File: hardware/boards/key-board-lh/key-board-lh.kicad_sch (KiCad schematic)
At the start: 24 parts

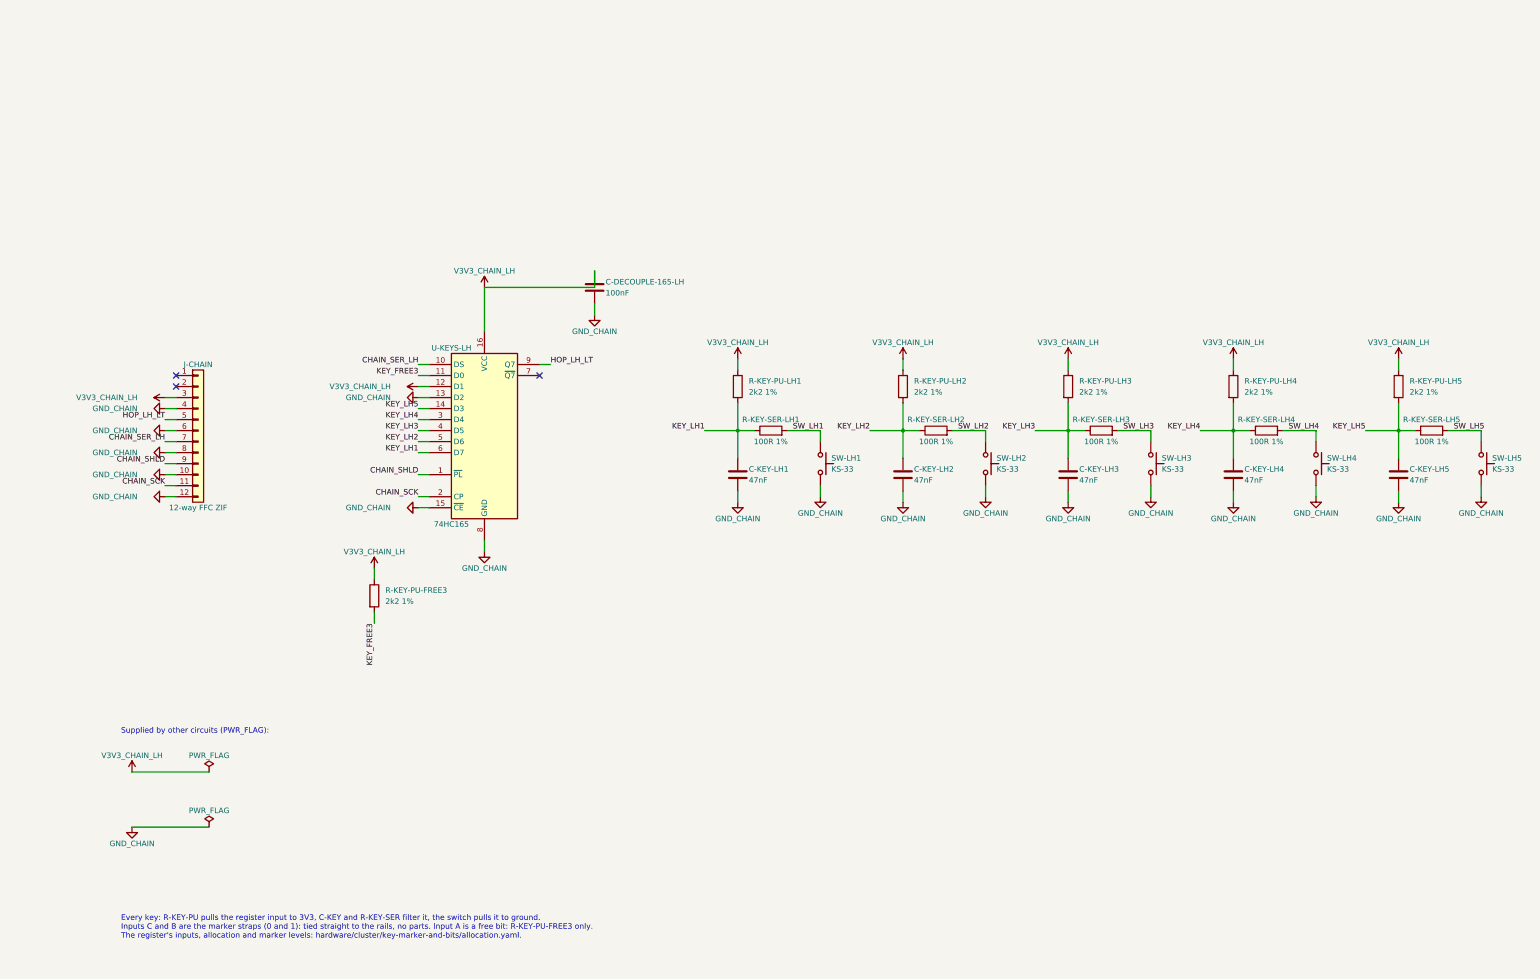
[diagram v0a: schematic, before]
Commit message: KiCad sheets are the source of truth (ADR 0019): key-board circuits and boards migrated
- The circuit sheets key-register, key-switch-network and
  key-marker-and-bits own their connections and part facts (fields Row,
  Pins, Pins_source, Note; ports as hierarchical labels). Their
  netlist.yaml is now EXPORTED by tools/kicad.py.
- key-board-rh and key-board-lh are KiCad projects placing those sheets
  once per instance (register, one per key, one per free bit); their
  board-netlist.yaml is exported, with KiCad's ERC over the hierarchy.
- Proved: every exported circuit netlist equals the hand-written one it
  replaces, part by part and net by net; both KiCad boards equal the
  boards the retired tools/board.py assembled. ERC clean.
- key-marker-and-bits is now one free-bit pull-up, replicated 3; marker
  straps are board wiring. nets.yaml gains FREE_BIT.
- tools/kicad.py check: stale exports, stale or edited renders
  (hardware/SHEETS.csv), board ERC, and board wiring vs allocation.yaml vs
  the page table vs key-layout.yaml. Tested: an unexported edit and a
  swapped key both fail.
- CLAUDE.md, hardware/README.md, repo-maintenance.md and tooling.md say
  what is source and what is exported. tools/board.py retired.

Co-Authored-By: Claude Opus 5.5 <noreply@anthropic.com>
Claude-Session: https://claude.ai/code/session_01LmB4muFXnoLprWX4JzuJ5A
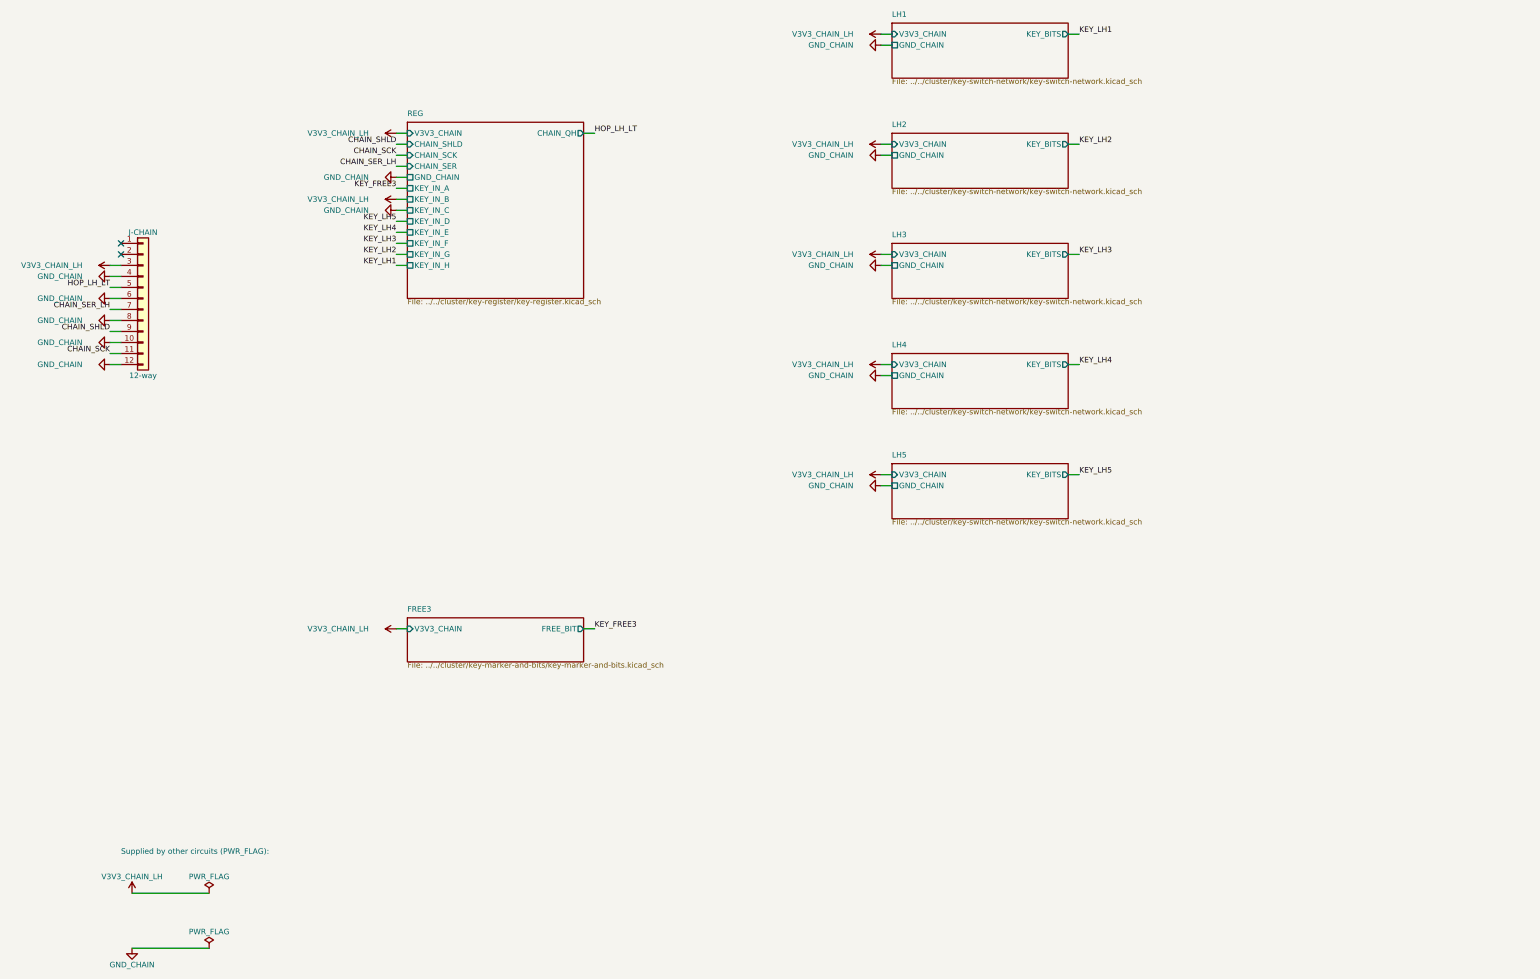
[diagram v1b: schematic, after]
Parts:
- removed C-DECOUPLE-165-LH: 100nF, symbol Device:C
- removed C-KEY-LH1, C-KEY-LH2, C-KEY-LH3, C-KEY-LH4, C-KEY-LH5: 47nF, symbol Device:C
- removed R-KEY-PU-FREE3, R-KEY-PU-LH1, R-KEY-PU-LH2, R-KEY-PU-LH3, R-KEY-PU-LH4, R-KEY-PU-LH5: 2k2 1%, symbol Device:R
- removed R-KEY-SER-LH1, R-KEY-SER-LH2, R-KEY-SER-LH3, R-KEY-SER-LH4, R-KEY-SER-LH5: 100R 1%, symbol Device:R
- removed SW-LH1, SW-LH2, SW-LH3, SW-LH4, SW-LH5: KS-33, symbol Switch:SW_Push
- removed U-KEYS-LH: 74HC165, symbol 74xx:74HC165
- J-CHAIN: value 12-way FFC ZIF -> 12-way; Note (none) -> left_hand key board. REVERSED, like the right_hand one; Pins (none) -> 1=1 2=2 3=3 4=4 5=5 6=6 7=7 8=8 9=9 10=10 11=11 12=12; Row (none) -> J-CHAIN
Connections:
- no-connect marks 3 -> 2
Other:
- added sheet FREE3 (../../cluster/key-marker-and-bits/key-marker-and-bits.kicad_sch)
- added sheet LH1 (../../cluster/key-switch-network/key-switch-network.kicad_sch)
- added sheet LH2 (../../cluster/key-switch-network/key-switch-network.kicad_sch)
- added sheet LH3 (../../cluster/key-switch-network/key-switch-network.kicad_sch)
- added sheet LH4 (../../cluster/key-switch-network/key-switch-network.kicad_sch)
- added sheet LH5 (../../cluster/key-switch-network/key-switch-network.kicad_sch)
- added sheet REG (../../cluster/key-register/key-register.kicad_sch)
- note removed: "Every key: R-KEY-PU pulls the register input to 3V3, C-KEY and R-KEY-SER filter it, the switch pulls it to ground. Inputs C and B are the marker straps (0 and 1): tied straight to the rails, no parts. Input A is a free bit: R-KEY-PU-FREE3 only. The register's inputs, allocation and marker levels: hardware/cluster/key-marker-and-bits/allocation.yaml."
- title: Left-hand key board (PCB-CLUSTER, left_hand) -> Left-hand key board (left_hand cluster, PCB-CLUSTER)
- moved on the sheet: J-CHAIN

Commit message: First PCB: the left-hand key board, placed from the body CAD and routed
- tools/pcb.py: a board's first layout from its KiCad sheets (netlist,
  footprints) and the body CAD's new exports (key-board outline DXF,
  switch and ribbon-connector positions); then the .kicad_pcb is source.
  check = KiCad DRC with schematic parity + switches where the CAD puts
  them; render = 3D both sides, 2D copper, and fab/ (Gerbers, drill,
  placement), ledgered in hardware/SHEETS.csv. tools/kicad.py check runs it.
- tools/pcb_route.py: a small two-layer grid router for simple boards;
  ground routed as a net plus pours and stitching vias.
- key-board-lh: 24 parts, all nets routed; KiCad DRC 0 errors, schematic
  parity clean (one stock-footprint silkscreen warning). Tested: a switch
  moved 1 mm fails the check.
- Footprints on the sheets; hardware/lib/woody.pretty holds the KS-33
  footprint (marbastlib, banked) with Gateron's STEP lifted by
  switch.pcb_below_seat. J-CHAIN's stand-in is Molex 200528-0120.
- Findings, recorded in tooling.md §4 and DESIGN.md: the ribbon connector
  needs 6.7 mm, the CAD envelope is 5.5; KS-33 pins show only ~0.1 mm
  below a 1.6 mm board (1.2 mm would leave ~0.5).
- setup-env.sh installs footprints, rsvg, shapely and repairs an empty
  global fp-lib-table.

Co-Authored-By: Claude Opus 5.5 <noreply@anthropic.com>
Claude-Session: https://claude.ai/code/session_01LmB4muFXnoLprWX4JzuJ5A
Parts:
- J-CHAIN: footprint (none) -> Connector_FFC-FPC:Molex_200528-0120_1x12-1MP_P1.00mm_Horizontal
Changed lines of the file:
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@@
     (property "Reference" "J-CHAIN" (at 45.72 86.36 0) (effects (font (size 1.27 1.27))))
     (property "Value" "12-way" (at 45.72 119.38 0) (effects (font (size 1.27 1.27))))
-    (property "Footprint" "" (at 45.72 101.6 0) (effects (font (size 1.27 1.27)) hide))
+    (property "Footprint" "Connector_FFC-FPC:Molex_200528-0120_1x12-1MP_P1.00mm_Horizontal" (at 45.72 101.6 0) (effects (font (size 1.27 1.27)) hide))
     (property "Datasheet" "" (at 45.72 101.6 0) (effects (font (size 1.27 1.27)) hide))
     (property "Row" "J-CHAIN" (at 45.72 101.6 0) (effects (font (size 1.27 1.27)) hide))

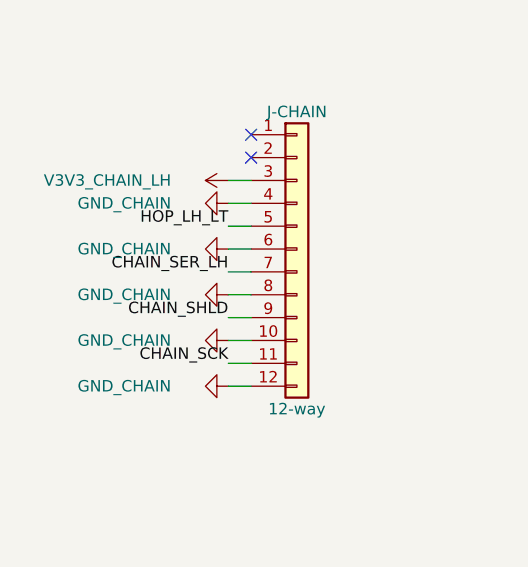
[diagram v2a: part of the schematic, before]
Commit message: Key chain on through-hole 1.27 mm IDC: model, key boards, router fix
The owner's choice (option 2): a right-angle 2x6 1.27 mm shrouded IDC header
on each board (Samtec SHF-106-01-L-D-RA stand-in), the key board's hanging
over the main board's, and a flat IDC ribbon long enough to plug in with the
lid laid beside the body - closed, a flat hairpin along the body, clear of
the LED strip.

- CAD: chain headers, plugs and the hairpin ribbon replace the ZIF/FFC C;
  positions found clear of every switch's pole and pins and the regulator
  block; ribbon length derived from the service position (drc.echo); a plate
  window over the key header's pin tails. body.yaml boards.chain_* and
  routing.chain_* replace ffc_*. 0 DRC FAILs, 0 clashes over 134 solids.
- Key boards: J-CHAIN footprint woody:IDC-Header_2x06_P1.27mm_Samtec_SHF_
  Horizontal (new); pinout moved one pin for the upside-down header (main
  pin n -> key pin 12-n odd / 14-n even); ERC clean. The interface netlist
  follows and agrees pin for pin.
- pcb.py places J-CHAIN from the CAD's "chain" line and checks it; the
  router no longer walls a plated pad off from its own track (1.27 mm pads).
  LH board: DRC 0 errors, parity clean; renders and fab/ regenerated.

The BOM rows, the key-chain page and the ADR 0017 amendment follow in the
next commit.

Co-Authored-By: Claude Opus 5.5 <noreply@anthropic.com>
Claude-Session: https://claude.ai/code/session_01LmB4muFXnoLprWX4JzuJ5A
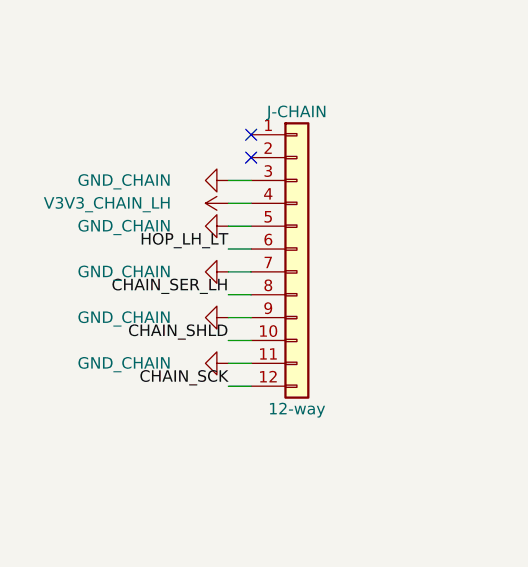
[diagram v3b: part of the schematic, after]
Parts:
- J-CHAIN: footprint Connector_FFC-FPC:Molex_200528-0120_1x12-1MP_P1.00mm_Horizontal -> woody:IDC-Header_2x06_P1.27mm_Samtec_SHF_Horizontal; Note left_hand key board. REVERSED, like the right_hand one -> key-board end of the chain ribbon: 1.27 mm IDC, right-angle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
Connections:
- net CHAIN_SCK: now also J-CHAIN.12 (Pin_12); no longer J-CHAIN.11 (Pin_11)
- net CHAIN_SER_LH: now also J-CHAIN.8 (Pin_8); no longer J-CHAIN.7 (Pin_7)
- net CHAIN_SHLD: now also J-CHAIN.10 (Pin_10); no longer J-CHAIN.9 (Pin_9)
- net GND_CHAIN: now also J-CHAIN.11 (Pin_11), J-CHAIN.3 (Pin_3), J-CHAIN.5 (Pin_5), J-CHAIN.7 (Pin_7), J-CHAIN.9 (Pin_9); no longer J-CHAIN.10 (Pin_10), J-CHAIN.12 (Pin_12), J-CHAIN.4 (Pin_4), J-CHAIN.6 (Pin_6), J-CHAIN.8 (Pin_8)
- net HOP_LH_LT: now also J-CHAIN.6 (Pin_6); no longer J-CHAIN.5 (Pin_5)
- net V3V3_CHAIN_LH: now also J-CHAIN.4 (Pin_4); no longer J-CHAIN.3 (Pin_3)

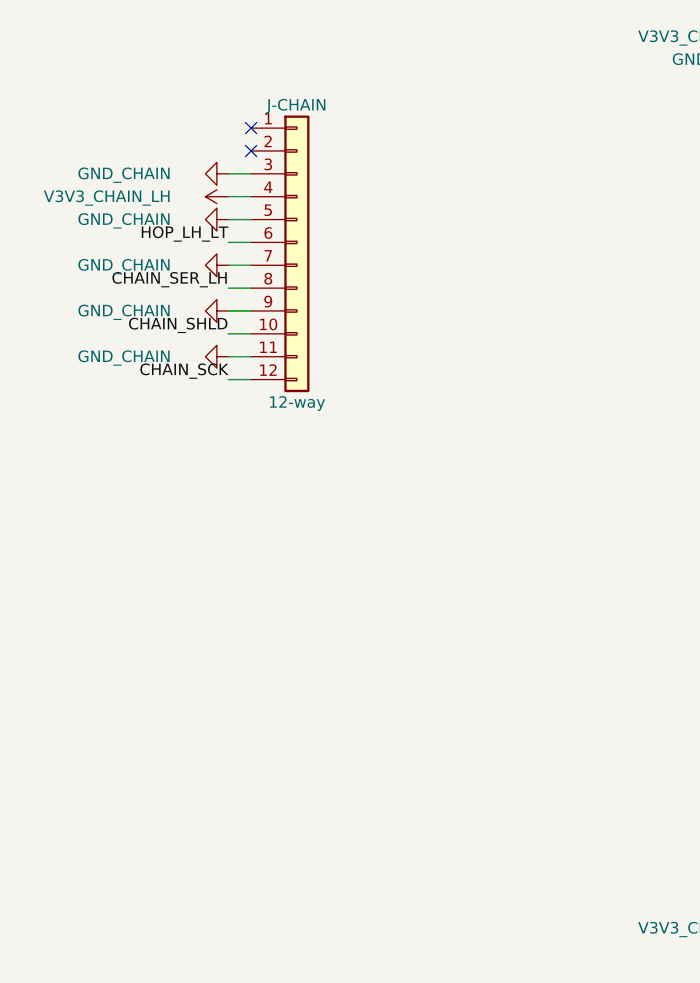
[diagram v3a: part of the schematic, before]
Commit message: LH key board as the worked example: orderable, labelled, testable
- Samtec full prints banked (SHF header, FFSD cable); the header's true
  dimensions replace the catalogue estimates (body.yaml boards.chain_*), and
  the cable is ordered -RN2 (notch reversed on the key-board end): both
  sockets' cables leave downward, the ribbon runs flat, and key-board pin =
  13 - main-board pin. The same-day 12-n/14-n map was wrong and is undone in
  the sheets, the interface netlist and the docs (history in notes.md).
- Model: the hairpin's legs follow the cable's real exit - the main board's
  on the board, clear of the thumb switches' poles; 0 DRC FAILs, 0 clashes.
- Sheets: Manufacturer/MPN/LCSC/Assembly fields from JLC's parts API (JLC
  and LCSC pages banked in datasheets/fab and the manifest); five bring-up
  test pads per key board (TP-CHAIN, copper only).
- pcb.py: JLC's limits in the DRC (layout.yaml fab:), which grew the vias
  and J-CHAIN's pads to the 0.18 mm ring; HASL lead-free in the stackup and
  Gerber job; a generated parts-side silkscreen; the JLC BOM, CPL and
  hand-assembly list in fab/, ledgered against board and sheets.
- Router: a real rip-up (blockers removed too); plated holes no longer wall
  off their own pads.
- hardware/boards/key-board-lh/README.md: sources, ordering, hand assembly,
  bring-up, open items. tooling.md and lib README follow.
All checks pass: CAD, DRC (0/0), KiCad, staleness, BOM, netlist, datasheets.

Co-Authored-By: Claude Opus 5.5 <noreply@anthropic.com>
Claude-Session: https://claude.ai/code/session_01LmB4muFXnoLprWX4JzuJ5A
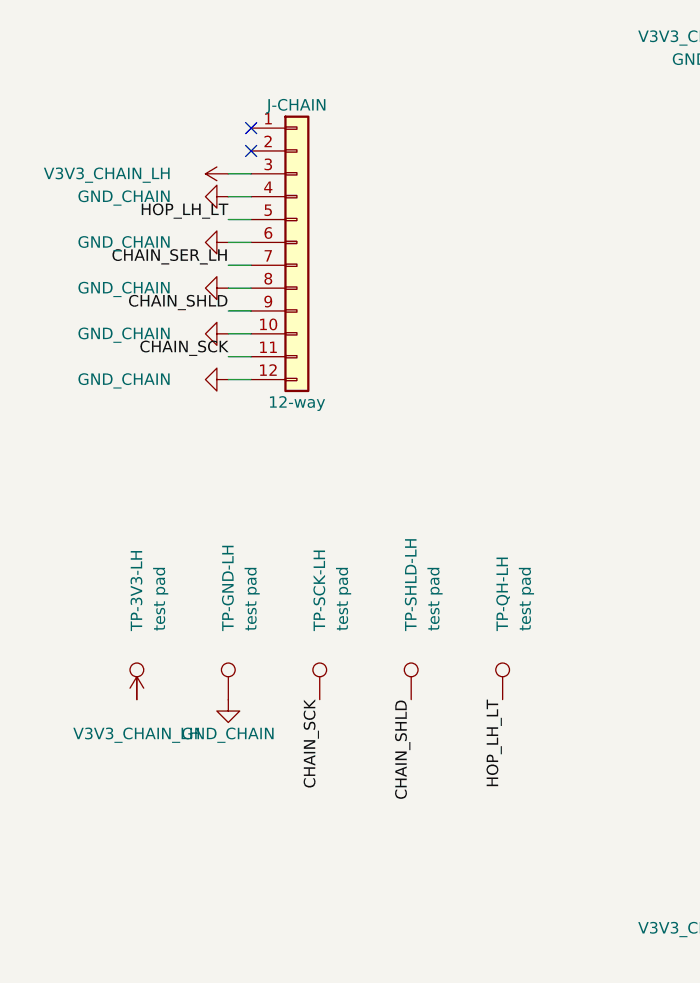
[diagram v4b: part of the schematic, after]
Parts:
- added TP-3V3-LH, TP-GND-LH, TP-QH-LH, TP-SCK-LH, TP-SHLD-LH: test pad, TestPoint:TestPoint_Pad_D1.0mm, symbol Connector:TestPoint
- J-CHAIN: Assembly (none) -> hand; MPN (none) -> SHF-106-01-L-D-RA; Manufacturer (none) -> Samtec; Note key-board end of the chain ribbon: 1.27 mm IDC, right-angle, upside down on the underside, so main-board pin n arrives at pin 12-n (n odd) or 14-n (n even) - key-chain-loom.md, ADR 0017 amended -> key-board end of the chain ribbon: 1.27 mm IDC, right-angle, upside down on the underside; the cable's key-board socket has its notch reversed (FFSD -RN2), so main-board pin n arrives at pin 13-n - key-chain-loom.md
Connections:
- net CHAIN_SCK: now also J-CHAIN.11 (Pin_11), TP-SCK-LH.1; no longer J-CHAIN.12 (Pin_12)
- net CHAIN_SER_LH: now also J-CHAIN.7 (Pin_7); no longer J-CHAIN.8 (Pin_8)
- net CHAIN_SHLD: now also J-CHAIN.9 (Pin_9), TP-SHLD-LH.1; no longer J-CHAIN.10 (Pin_10)
- net GND_CHAIN: now also J-CHAIN.10 (Pin_10), J-CHAIN.12 (Pin_12), J-CHAIN.4 (Pin_4), J-CHAIN.6 (Pin_6), J-CHAIN.8 (Pin_8), TP-GND-LH.1; no longer J-CHAIN.11 (Pin_11), J-CHAIN.3 (Pin_3), J-CHAIN.5 (Pin_5), J-CHAIN.7 (Pin_7), J-CHAIN.9 (Pin_9)
- net HOP_LH_LT: now also J-CHAIN.5 (Pin_5), TP-QH-LH.1; no longer J-CHAIN.6 (Pin_6)
- net V3V3_CHAIN_LH: now also J-CHAIN.3 (Pin_3), TP-3V3-LH.1; no longer J-CHAIN.4 (Pin_4)

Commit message: WIP: layout-side fixes (networks as T, via-in-pad, segment merge, silk, stackup, TP-SER, drills)
Co-Authored-By: Claude Opus 5.5 <noreply@anthropic.com>
Claude-Session: https://claude.ai/code/session_01LmB4muFXnoLprWX4JzuJ5A
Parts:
- added TP-SER-LH: test pad, TestPoint:TestPoint_Pad_D1.0mm, symbol Connector:TestPoint
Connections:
- net CHAIN_SER_LH: now also TP-SER-LH.1
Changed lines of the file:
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@@
   )
   (label "HOP_LH_LT" (at 68.58 152.4 270) (fields_autoplaced) (effects (font (size 1.27 1.27)) (justify right bottom)))
+  (symbol (lib_id "Connector:TestPoint") (at 78.74 152.4 0) (unit 1)
+    (in_bom no) (on_board yes) (dnp no)
+    (property "Reference" "TP-SER-LH" (at 78.74 144.78 90) (effects (font (size 1.27 1.27)) (justify left)))
+    (property "Value" "test pad" (at 81.28 144.78 90) (effects (font (size 1.27 1.27)) (justify left)))
+    (property "Footprint" "TestPoint:TestPoint_Pad_D1.0mm" (at 78.74 152.4 0) (effects (font (size 1.27 1.27)) hide))
+    (property "Datasheet" "" (at 78.74 152.4 0) (effects (font (size 1.27 1.27)) hide))
+    (property "Row" "TP-CHAIN" (at 78.74 152.4 0) (effects (font (size 1.27 1.27)) hide))
+    (property "Pins" "1=1" (at 78.74 152.4 0) (effects (font (size 1.27 1.27)) hide))
+    (property "Note" "bring-up test pad: this board's serial input (SER), driven by the next board up the chain - tie it to TP-GND or TP-3V3 on the bench, where nothing drives it (hardware/boards/key-board-lh/README.md)" (at 78.74 152.4 0) (effects (font (size 1.27 1.27)) hide))
+    (property "Assembly" "none" (at 78.74 152.4 0) (effects (font (size 1.27 1.27)) hide))
+    (pin "1")
+    (instances (project "key-board-lh" (path "/a2d77fad-366b-59d5-8d08-ccdc7dd94a07" (reference "TP-SER-LH") (unit 1))))
+  )
+  (label "CHAIN_SER_LH" (at 78.74 152.4 270) (fields_autoplaced) (effects (font (size 1.27 1.27)) (justify right bottom)))
   (sheet_instances (path "/" (page "1")))
 )
